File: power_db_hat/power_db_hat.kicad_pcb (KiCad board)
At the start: 2 copper layers, 65 x 56 mm, 161 parts, among them J1 GPIO, J10 Conn_01x04_Pin, J2 BAT1, J3 12V_out, J4 Conn_01x04_Pin, J5 24V_out, J6 PD_power, J7 Conn_01x20_Pin, J8 BAT2, J9 Conn_01x04_Pin, Q1 PMOS, Q2 PMOS, Q3 PMOS, Q5 PMOS, U1 INA3221, U2 TL431DBZ, U3 TPS54560BDDA, U4 TL431DBZ

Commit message: lol
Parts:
- removed C1, C10, C12, C18, C2, C3, C4, C5: 100nF, Capacitor_SMD:C_0805_2012Metric_Pad1.18x1.45mm_HandSolder
- removed D10, D14, D17, D18, D19, D20, D21, D22, D23, D24, D25, D26, D27, D28, D29, D30, D31, D32, D33, D34, D35, D36, D37, D38, D45, D46, D48, D50: TVS_3V3, Diode_SMD:D_0603_1608Metric_Pad1.05x0.95mm_HandSolder
- removed D11, D12, D13, D42, D9: TVS_13V, Diode_SMD:D_0603_1608Metric_Pad1.05x0.95mm_HandSolder
- removed D15, D16, D43, D8: TVS_26V, Diode_SMD:D_0603_1608Metric_Pad1.05x0.95mm_HandSolder
- removed D44, D47, D49, D51: TVS_5V, Diode_SMD:D_0603_1608Metric_Pad1.05x0.95mm_HandSolder
- removed F1: FUSE_10A, Fuse:Fuse_2512_6332Metric_Pad1.52x3.35mm_HandSolder
- removed F2: FUSE_5A, Fuse:Fuse_2512_6332Metric_Pad1.52x3.35mm_HandSolder
- removed J3: 12V_out, CONN_AMASS_3D_FIXED:AMASS_XT60PW-F_1x02_P7.20mm_Horizontal
- removed JP1, JP2, JP3, JP4: SolderJumper_2_Open, Jumper:SolderJumper-2_P1.3mm_Open_TrianglePad1.0x1.5mm
- removed L1: 8.2uH, Inductors_custom:VSHB0754T_Molded_Power_Choke
- removed Q1, Q2, Q5: PMOS, Package_TO_SOT_SMD:TO-252-3_TabPin2
- removed R1, R2, R3, R4: 0, Resistor_SMD:R_0603_1608Metric_Pad0.98x0.95mm_HandSolder
- removed R10, R11, R12, R13, R14: R, Resistor_SMD:R_0603_1608Metric_Pad0.98x0.95mm_HandSolder
- removed R15, R17: 12k, Resistor_SMD:R_0603_1608Metric_Pad0.98x0.95mm_HandSolder
- removed R16: 3k, Resistor_SMD:R_0603_1608Metric_Pad0.98x0.95mm_HandSolder
- removed R18, R28: 100, Resistor_SMD:R_0603_1608Metric_Pad0.98x0.95mm_HandSolder
- removed R21: 75k, Resistor_SMD:R_0603_1608Metric_Pad0.98x0.95mm_HandSolder
- removed R24: 2.2k, Resistor_SMD:R_0603_1608Metric_Pad0.98x0.95mm_HandSolder
- removed R25: 68k, Resistor_SMD:R_0603_1608Metric_Pad0.98x0.95mm_HandSolder
- removed R26, R6: 10k, Resistor_SMD:R_0603_1608Metric_Pad0.98x0.95mm_HandSolder
- removed R27, R32, R37, R39, R40, R41: 4.7k, Resistor_SMD:R_0603_1608Metric_Pad0.98x0.95mm_HandSolder
- removed R29: 200k, Resistor_SMD:R_0603_1608Metric_Pad0.98x0.95mm_HandSolder
- removed R45, R46, R47, R48, R49, R50, R51, R52, R53, R54, R55, R56, R57, R58, R59, R60, R61, R62, R63, R64: 33, Resistor_SMD:R_0603_1608Metric_Pad0.98x0.95mm_HandSolder
- removed R5, R7: 100k, Resistor_SMD:R_0603_1608Metric_Pad0.98x0.95mm_HandSolder
- removed U4: TL431DBZ, Package_TO_SOT_SMD:SOT-23
- added C27: 22uF, Capacitor_SMD:C_0603_1608Metric_Pad1.08x0.95mm_HandSolder, B.Cu at (141.3, 58.0)
- added C28: 22uF, Capacitor_SMD:C_0603_1608Metric_Pad1.08x0.95mm_HandSolder, B.Cu at (141.3, 60.5)
- added C29: 100nF, Capacitor_SMD:C_0603_1608Metric_Pad1.08x0.95mm_HandSolder, B.Cu at (141.3, 63.0)
- added C31: 100nF, Capacitor_SMD:C_0603_1608Metric_Pad1.08x0.95mm_HandSolder, B.Cu at (141.3, 65.5)
- added C32: 2.2uF, Capacitor_SMD:C_0603_1608Metric_Pad1.08x0.95mm_HandSolder, B.Cu at (141.3, 68.0)
- added C33: 22uF, Capacitor_SMD:C_0603_1608Metric_Pad1.08x0.95mm_HandSolder, B.Cu at (141.3, 70.6)
- added C34: 2.2uF, Capacitor_SMD:C_0603_1608Metric_Pad1.08x0.95mm_HandSolder, B.Cu at (137.0, 53.0)
- added C35: 100nF, Capacitor_SMD:C_0603_1608Metric_Pad1.08x0.95mm_HandSolder, B.Cu at (137.0, 55.5)
- added C36: 22nF, Capacitor_SMD:C_0603_1608Metric_Pad1.08x0.95mm_HandSolder, B.Cu at (137.0, 58.0)
- added C37: 100nF, Capacitor_SMD:C_0603_1608Metric_Pad1.08x0.95mm_HandSolder, B.Cu at (137.0, 60.5)
- added C38: 100nF, Capacitor_SMD:C_0603_1608Metric_Pad1.08x0.95mm_HandSolder, B.Cu at (137.0, 63.0)
- added C39: 22uF, Capacitor_SMD:C_0603_1608Metric_Pad1.08x0.95mm_HandSolder, B.Cu at (137.0, 65.5)
- added C40: 2.2uF, Capacitor_SMD:C_0603_1608Metric_Pad1.08x0.95mm_HandSolder, B.Cu at (137.0, 68.0)
- added C41: 22uF, Capacitor_SMD:C_0603_1608Metric_Pad1.08x0.95mm_HandSolder, B.Cu at (137.0, 70.6)
- added C42: 22uF, Capacitor_SMD:C_0603_1608Metric_Pad1.08x0.95mm_HandSolder, B.Cu at (132.6, 53.0)
- added C43: 22uF, Capacitor_SMD:C_0603_1608Metric_Pad1.08x0.95mm_HandSolder, B.Cu at (132.6, 55.5)
- added D52: D_Schottky, Diode_SMD:D_SMA-SMB_Universal_Handsoldering, B.Cu at (153.5, 83.1)
- added J11: Conn_01x03_Pin, Connector:FanPinHeader_1x03_P2.54mm_Vertical, F.Cu at (144.5, 48.0)
- added J12: Conn_01x03_Pin, Connector:FanPinHeader_1x03_P2.54mm_Vertical, F.Cu at (155.0, 48.0)
- added J15: Screw_Terminal_01x02, TerminalBlock:TerminalBlock_Xinya_XY308-2.54-2P_1x02_P2.54mm_Horizontal, F.Cu at (134.8, 48.3)
- added J16: Screw_Terminal_01x02, TerminalBlock:TerminalBlock_Xinya_XY308-2.54-2P_1x02_P2.54mm_Horizontal, F.Cu at (117.0, 95.5)
- added J17: Conn_02x06_Counter_Clockwise, Connector_PinSocket_2.54mm:PinSocket_2x06_P2.54mm_Vertical_SMD, B.Cu at (108.5, 85.5)
- added Q6: SIS468DN, Package_SO:Vishay_PowerPAK_1212-8_Single, B.Cu at (123.2, 54.2)
- added Q7: SIS468DN, Package_SO:Vishay_PowerPAK_1212-8_Single, B.Cu at (123.2, 58.9)
- added R65: 0, Resistor_SMD:R_0603_1608Metric_Pad0.98x0.95mm_HandSolder, B.Cu at (128.3, 68.0)
- added R66: 0, Resistor_SMD:R_0603_1608Metric_Pad0.98x0.95mm_HandSolder, B.Cu at (128.3, 70.6)
- added TP1: TestPoint, TestPoint:TestPoint_Pad_D1.0mm, F.Cu at (110.0, 50.0)
- added TP2: TestPoint, TestPoint:TestPoint_Pad_D1.0mm, F.Cu at (112.5, 50.0)
- added TP3: TestPoint, TestPoint:TestPoint_Pad_D1.0mm, F.Cu at (115.0, 50.0)
- added TP4: TestPoint, TestPoint:TestPoint_Pad_D1.0mm, F.Cu at (117.5, 50.0)
- added U5: MAX17506ATP+T, MAX17506:21-0140L_T2055-4_MXM, B.Cu at (126.5, 82.5)
- added U6: LDD-700LS, LD-700LS:SOP254P1280X930-16N, F.Cu at (141.1, 76.4)
- C11: value 4.7nF -> 2.2uF; moved to B.Cu
- C13: value 47pF -> 22uF; moved to B.Cu
- C14: value 100nF -> 2.2uF; footprint Capacitor_SMD:C_0805_2012Metric_Pad1.18x1.45mm_HandSolder -> Capacitor_SMD:C_0603_1608Metric_Pad1.08x0.95mm_HandSolder; moved to B.Cu
- C15: value 47uF -> 22nF; moved to B.Cu
- C16: value 47uF -> 100nF; moved to B.Cu
- C17: value 47uF -> 22uF; moved to B.Cu
- C6, C9: value 2.2uF -> 100nF; moved to B.Cu
- C7: moved to B.Cu
- C8: value 2.2uF -> 22uF; moved to B.Cu
- D1: value 3V3 -> LED_R; moved to F.Cu
- D2: value 5V -> LED_R; moved to F.Cu
- D3: value 12V -> LED_R; moved to F.Cu
- D4: value 24V -> LED_R; moved to F.Cu
- D5: value LED -> LED_R; moved to F.Cu
- D6: value B560C -> D_Schottky; footprint Diode_SMD:D_SMB-SMC_Universal_Handsoldering -> Diode_SMD:D_SMA-SMB_Universal_Handsoldering
- D7: value 12V -> TVS_26V
- J1: value GPIO -> Conn_01x02_Pin; footprint Connector_PinSocket_2.54mm:PinSocket_2x20_P2.54mm_Vertical -> TerminalBlock:TerminalBlock_Xinya_XY308-2.54-2P_1x02_P2.54mm_Horizontal; moved to F.Cu
- J10: value Conn_01x04_Pin -> Screw_Terminal_01x02; footprint Connector_JST:JST_GH_SM04B-GHS-TB_1x04-1MP_P1.25mm_Horizontal -> TerminalBlock:TerminalBlock_Xinya_XY308-2.54-2P_1x02_P2.54mm_Horizontal
- J2, J8: footprint CONN_AMASS_3D_FIXED:AMASS_XT60PW-M_1x02_P7.20mm_Horizontal -> AMASS_Custom:AMASS_XT60PW-M_1x02_P7.20mm_Horizontal
- J4: value Conn_01x04_Pin -> Screw_Terminal_01x02; footprint Connector_JST:JST_SH_SM04B-SRSS-TB_1x04-1MP_P1.00mm_Horizontal -> TerminalBlock:TerminalBlock_Xinya_XY308-2.54-2P_1x02_P2.54mm_Horizontal
- J5: footprint CONN_AMASS_3D_FIXED:AMASS_XT60PW-F_1x02_P7.20mm_Horizontal -> AMASS_Custom:AMASS_XT60PW-F_1x02_P7.20mm_Horizontal
- J6: value PD_power -> Conn_01x02_Pin; footprint Connector_JST:JST_GH_SM04B-GHS-TB_1x04-1MP_P1.25mm_Horizontal -> TerminalBlock:TerminalBlock_Xinya_XY308-2.54-2P_1x02_P2.54mm_Horizontal
- J7: value Conn_01x20_Pin -> Conn_02x06_Counter_Clockwise; footprint Connector_PinHeader_1.00mm:PinHeader_1x20_P1.00mm_Vertical -> Connector_PinSocket_2.54mm:PinSocket_2x06_P2.54mm_Vertical_SMD; moved to B.Cu
- J9: value Conn_01x04_Pin -> Conn_02x06_Counter_Clockwise; footprint Connector_JST:JST_GH_SM04B-GHS-TB_1x04-1MP_P1.25mm_Horizontal -> Connector_PinSocket_2.54mm:PinSocket_2x06_P2.54mm_Vertical_SMD; moved to B.Cu
- Q3: value PMOS -> AO4407A; footprint Package_TO_SOT_SMD:TO-252-3_TabPin2 -> Package_SO:SOIC-8-1EP_3.9x4.9mm_P1.27mm_EP2.41x3.81mm; moved to B.Cu
- R19: value 309k -> 4.7R; moved to B.Cu
- R20: value 53.6k -> 4.7R; moved to B.Cu
- R22: value 309k -> 162k; moved to B.Cu
- R23: value 14k -> 33.2k; moved to B.Cu
- R30: value 53.6k -> 10k; moved to B.Cu
- R31: value 10.2k -> 0; moved to B.Cu
- R35: value 4.7k -> 309k; moved to B.Cu
- R36: value 4.7k -> 24.9k; moved to B.Cu
- R38: value 4.7k -> 10k; moved to B.Cu
- R42, R43: value 33 -> 4.7R; moved to B.Cu
- R44: value 33 -> 0; moved to B.Cu
- U2: value TL431DBZ -> LDD-700LS; footprint Package_TO_SOT_SMD:SOT-23 -> LD-700LS:SOP254P1280X930-16N; moved to F.Cu
- U3: value TPS54560BDDA -> MAX17506ATP+T; footprint Package_SO:Texas_R-PDSO-G8_EP2.95x4.9mm_Mask2.4x3.1mm_ThermalVias -> MAX17506:21-0140L_T2055-4_MXM; moved to B.Cu
- moved D1 132.8 mm to (110.0, 47.0), turned to -90 degrees
- moved D2 130.7 mm to (112.5, 47.0), turned to -90 degrees
- moved D3 128.6 mm to (115.0, 47.0), turned to -90 degrees
- moved D4 126.6 mm to (117.5, 47.0), turned to -90 degrees
- moved D5 124.7 mm to (120.0, 47.0), turned to -90 degrees
- moved U2 121.7 mm to (142.2, 61.1), turned to 90 degrees
- moved R33 120.5 mm to (153.6, 70.0)
- moved R34 120.5 mm to (153.6, 74.9)
- moved R8 120.5 mm to (153.6, 65.1)
- moved U1 101.2 mm to (115.5, 66.5), turned to 0 degrees
- moved R38 84.3 mm to (128.3, 58.0), turned to 180 degrees
- moved R35 82.0 mm to (128.3, 53.0), turned to 180 degrees
- moved R36 82.0 mm to (128.3, 55.5), turned to 180 degrees
- moved R20 69.0 mm to (132.6, 60.5), turned to 180 degrees
- moved R23 68.2 mm to (132.6, 65.5), turned to 180 degrees
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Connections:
- C11 pad 1: GND -> /power/24V_SNS
- C11 pad 2: Net-(C11-Pad2) -> GND
- C13 pad 1: GND -> /power/24V_SNS
- C13 pad 2: Net-(U3-COMP) -> GND
- C14 pad 1: Net-(U3-BOOT) -> Net-(U3-VCC)
- C14 pad 2: Net-(D6-K) -> GND
- C15 pad 1: GND -> Net-(U3-SS)
- C15 pad 2: /power/5V_SNS -> GND
- C16 pad 1: GND -> Net-(U3-BST)
- C16 pad 2: /power/5V_SNS -> Net-(Q7-D)
- C17 pad 1: GND -> /power/bucks/BUCK_OUT_5V
- C17 pad 2: /power/5V_SNS -> GND
- C6 pad 1: /power/BUCK_IN -> /power/24V_SNS
- C7 pad 1: /power/BUCK_IN -> /power/24V_SNS
- C8 pad 1: /power/BUCK_IN -> /power/24V_SNS
- C9 pad 1: /power/BUCK_IN -> /power/24V_SNS
- D6 pad 1: Net-(D6-K) -> /power/5V_SNS
- D6 pad 2: GND -> /power/bucks/BUCK_OUT_5V
- J1 pad 1: +3V3 -> Net-(J1-Pin_1)
- J1 pad 2: +5V -> Net-(J1-Pin_2)
- J10 pad 1: /power/VIN_24V -> GND
- J10 pad 2: Net-(D16-A) -> GND
- J4 pad 1: GND -> +12V
- J4 pad 2: Net-(D36-K) -> GND
- J6 pad 1: /PD_VIN -> Net-(J6-Pin_1)
- J6 pad 2: GND -> Net-(J6-Pin_2)
- J7 pad 1: Net-(D14-K) -> GND
- J7 pad 10: Net-(D25-K) -> GND
- J7 pad 11: Net-(D26-K) -> GND
- J7 pad 12: Net-(D27-K) -> GND
- J7 pad 2: Net-(D17-K) -> /I2C_SDA
- J7 pad 3: Net-(D18-K) -> GND
- J7 pad 4: Net-(D19-K) -> GND
- J7 pad 5: Net-(D20-K) -> /IND_2
- J7 pad 6: Net-(D21-K) -> GND
- J7 pad 7: Net-(D22-K) -> /IND_3
- J7 pad 8: Net-(D23-K) -> GND
- J7 pad 9: Net-(D24-K) -> /IND_4
- J9 pad 1: /power/VIN_12V -> GND
- J9 pad 2: Net-(D13-K) -> /SERVO_1
- J9 pad 4: unconnected-(J9-Pin_4-Pad4) -> /SERVO_2
- R19 pad 1: /power/BUCK_IN -> Net-(U3-EXTVCC)
- R19 pad 2: Net-(U3-EN) -> /power/bucks/BUCK_OUT
- R20 pad 1: Net-(U3-EN) -> Net-(Q7-G)
- R20 pad 2: GND -> Net-(U3-DL)
- R22 pad 1: Net-(U3-RT/CLK) -> /power/bucks/BUCK_OUT_5V
- R22 pad 2: GND -> Net-(U3-FB)
- R23 pad 1: Net-(U3-COMP) -> Net-(U3-FB)
- R23 pad 2: Net-(C11-Pad2) -> GND
- R30 pad 1: /power/5V_SNS -> /power/bucks/BUCK_OUT_5V
- R30 pad 2: Net-(U3-FB) -> Net-(U3-*RESET)
- R31 pad 1: Net-(U3-FB) -> Net-(U3-EN/UVLO)
- R35 pad 1: /power/current/voltage_monitor/VDD -> /power/12V_SNS
- R35 pad 2: Net-(U1-SDA) -> Net-(U5-FB)
- R36 pad 1: /power/current/voltage_monitor/VDD -> Net-(U5-FB)
- R36 pad 2: Net-(U1-SCL) -> GND
- R38 pad 1: GND -> /power/12V_SNS
- R38 pad 2: Net-(U1-A0) -> Net-(U5-*RESET)
- R42 pad 1: /IVC_SW_2 -> Net-(U5-EXTVCC)
- R42 pad 2: Net-(D35-K) -> /power/12V_SNS
- R43 pad 1: /IVC_SW_1 -> Net-(Q6-G)
- R43 pad 2: Net-(D34-K) -> Net-(U5-DL)
- R44 pad 1: /IVC_SW_1_SOL -> Net-(U5-EN/UVLO)
- R44 pad 2: Net-(D33-K) -> GND
- U1 pad 16: /power/current/voltage_monitor/VDD -> +3V3
- U1 pad 5: Net-(U1-A0) -> Net-(JP5-A)
- U1 pad 6: Net-(U1-SCL) -> /I2C_SDA
- U1 pad 7: Net-(U1-SDA) -> GND
- U2 pad 1: Net-(U2-K) -> +24V
- U2 pad 2: Net-(U2-REF) -> Net-(J1-Pin_1)
- U2 pad 3: GND -> Net-(J1-Pin_1)
- U3 pad 1: Net-(U3-BOOT) -> /power/24V_SNS
- U3 pad 2: /power/BUCK_IN -> /power/24V_SNS
- U3 pad 3: Net-(U3-EN) -> GND
- U3 pad 4: Net-(U3-RT/CLK) -> Net-(U3-VCC)
- U3 pad 5: Net-(U3-FB) -> unconnected-(U3-MODE/SYNC-Pad5)
- U3 pad 6: Net-(U3-COMP) -> Net-(U3-*RESET)
- U3 pad 7: GND -> unconnected-(U3-RT-Pad7)
- U3 pad 8: Net-(D6-K) -> GND
- U3 pad 9: GND -> unconnected-(U3-CF-Pad9)
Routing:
- net /VBAT1+: track 13.8 -> 0.00 mm
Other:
- board text added: "24V"
- board text added: "BAT 1"
- board text added: "BAT 2"
- board text added: "LED1"
- board text added: "LED2"
- board text added: "SWITCH"
- board text added: "Servo1"
- board text added: "Servo2"
- board text removed: "DISPLAY (OPTIONAL)"

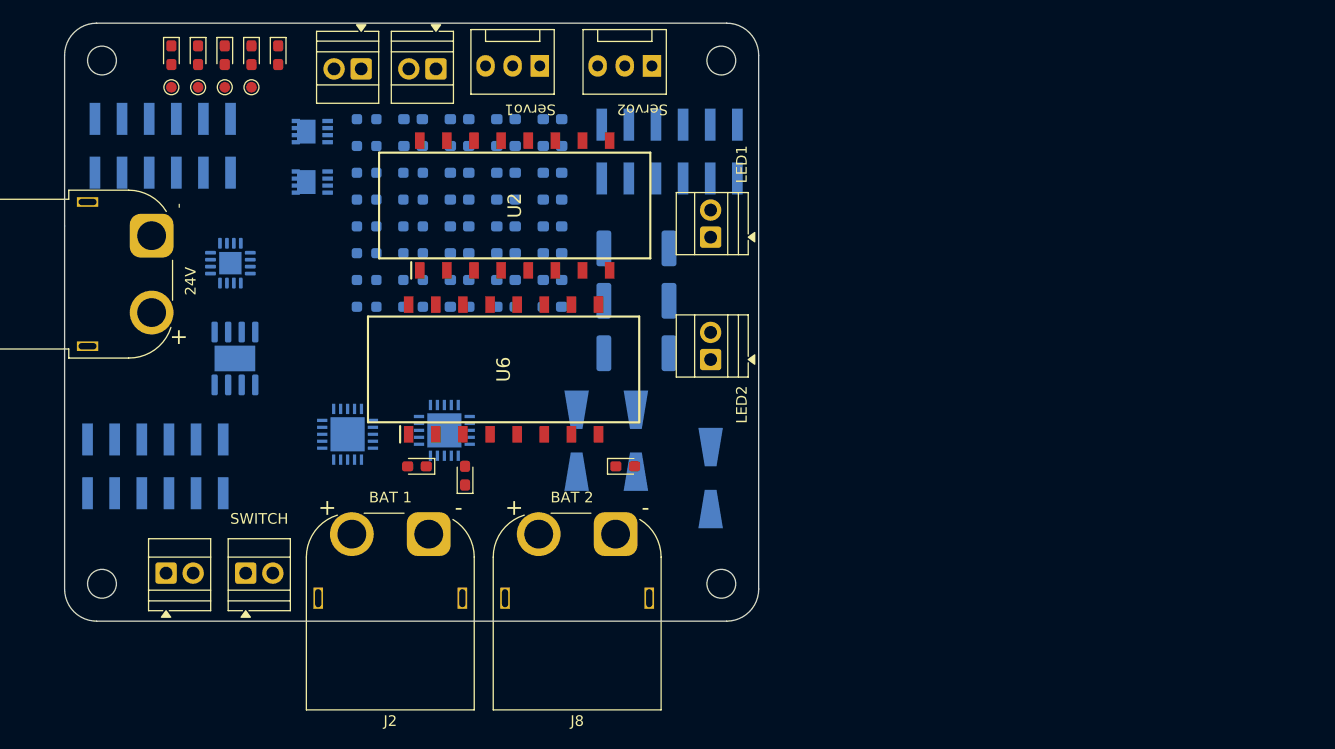
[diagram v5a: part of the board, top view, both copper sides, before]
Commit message: made b2b footprint
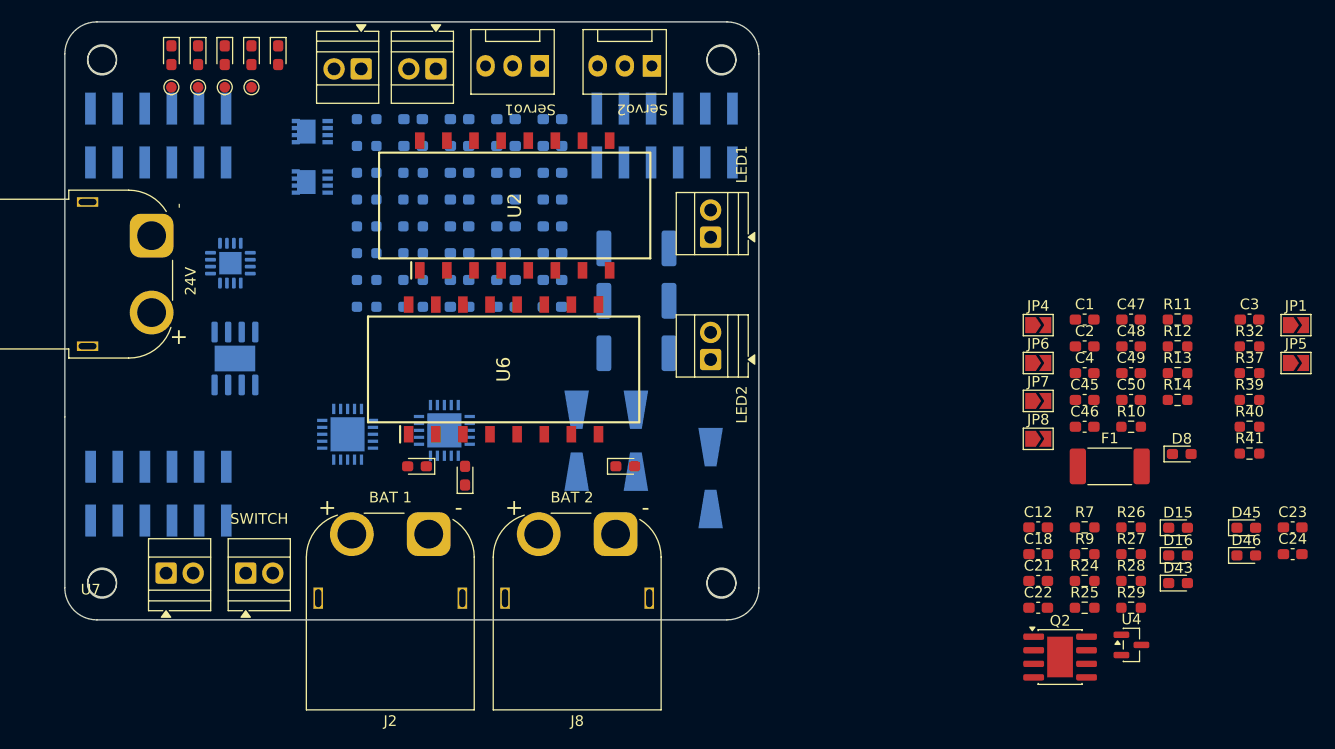
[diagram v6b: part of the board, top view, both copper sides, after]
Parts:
- removed J17, J7, J9: Conn_02x06_Counter_Clockwise, Connector_PinSocket_2.54mm:PinSocket_2x06_P2.54mm_Vertical_SMD
- added C1: 100nF, Capacitor_SMD:C_0603_1608Metric_Pad1.08x0.95mm_HandSolder, F.Cu at (195.5, 71.8)
- added C12: 100nF, Capacitor_SMD:C_0603_1608Metric_Pad1.08x0.95mm_HandSolder, F.Cu at (191.2, 91.2)
- added C18: 100nF, Capacitor_SMD:C_0603_1608Metric_Pad1.08x0.95mm_HandSolder, F.Cu at (191.2, 93.7)
- added C2: 100nF, Capacitor_SMD:C_0603_1608Metric_Pad1.08x0.95mm_HandSolder, F.Cu at (195.5, 74.3)
- added C21: 100nF, Capacitor_SMD:C_0603_1608Metric_Pad1.08x0.95mm_HandSolder, F.Cu at (191.2, 96.2)
- added C22: 100nF, Capacitor_SMD:C_0603_1608Metric_Pad1.08x0.95mm_HandSolder, F.Cu at (191.2, 98.7)
- added C23: 100nF, Capacitor_SMD:C_0603_1608Metric_Pad1.08x0.95mm_HandSolder, F.Cu at (215.0, 91.2)
- added C24: 100nF, Capacitor_SMD:C_0603_1608Metric_Pad1.08x0.95mm_HandSolder, F.Cu at (215.0, 93.7)
- added C3: 100nF, Capacitor_SMD:C_0603_1608Metric_Pad1.08x0.95mm_HandSolder, F.Cu at (211.0, 71.8)
- added C4: 100nF, Capacitor_SMD:C_0603_1608Metric_Pad1.08x0.95mm_HandSolder, F.Cu at (195.5, 76.8)
- added C45: 100nF, Capacitor_SMD:C_0603_1608Metric_Pad1.08x0.95mm_HandSolder, F.Cu at (195.5, 79.3)
- added C46: 22uF, Capacitor_SMD:C_0603_1608Metric_Pad1.08x0.95mm_HandSolder, F.Cu at (195.5, 81.8)
- added C47: 100nF, Capacitor_SMD:C_0603_1608Metric_Pad1.08x0.95mm_HandSolder, F.Cu at (199.9, 71.8)
- added C48: 22uF, Capacitor_SMD:C_0603_1608Metric_Pad1.08x0.95mm_HandSolder, F.Cu at (199.9, 74.3)
- added C49: 100nF, Capacitor_SMD:C_0603_1608Metric_Pad1.08x0.95mm_HandSolder, F.Cu at (199.9, 76.8)
- added C50: 22uF, Capacitor_SMD:C_0603_1608Metric_Pad1.08x0.95mm_HandSolder, F.Cu at (199.9, 79.3)
- added D15: TVS_26V, Diode_SMD:D_0603_1608Metric_Pad1.05x0.95mm_HandSolder, F.Cu at (204.3, 91.3)
- added D16: TVS_26V, Diode_SMD:D_0603_1608Metric_Pad1.05x0.95mm_HandSolder, F.Cu at (204.3, 93.8)
- added D43: TVS_26V, Diode_SMD:D_0603_1608Metric_Pad1.05x0.95mm_HandSolder, F.Cu at (204.3, 96.4)
- added D45: TVS_3V3, Diode_SMD:D_0603_1608Metric_Pad1.05x0.95mm_HandSolder, F.Cu at (210.7, 91.3)
- added D46: TVS_3V3, Diode_SMD:D_0603_1608Metric_Pad1.05x0.95mm_HandSolder, F.Cu at (210.7, 93.8)
- added D8: TVS_26V, Diode_SMD:D_0603_1608Metric_Pad1.05x0.95mm_HandSolder, F.Cu at (204.6, 84.3)
- added F1: FUSE_10A, Fuse:Fuse_2512_6332Metric_Pad1.52x3.35mm_HandSolder, F.Cu at (197.9, 85.5)
- added JP1: SolderJumper_2_Open, Jumper:SolderJumper-2_P1.3mm_Open_TrianglePad1.0x1.5mm, F.Cu at (215.3, 72.3)
- added JP4: SolderJumper_2_Open, Jumper:SolderJumper-2_P1.3mm_Open_TrianglePad1.0x1.5mm, F.Cu at (191.2, 72.3)
- added JP5: SolderJumper_2_Open, Jumper:SolderJumper-2_P1.3mm_Open_TrianglePad1.0x1.5mm, F.Cu at (215.3, 75.8)
- added JP6: SolderJumper_2_Open, Jumper:SolderJumper-2_P1.3mm_Open_TrianglePad1.0x1.5mm, F.Cu at (191.2, 75.8)
- added JP7: SolderJumper_2_Open, Jumper:SolderJumper-2_P1.3mm_Open_TrianglePad1.0x1.5mm, F.Cu at (191.2, 79.4)
- added JP8: SolderJumper_2_Open, Jumper:SolderJumper-2_P1.3mm_Open_TrianglePad1.0x1.5mm, F.Cu at (191.2, 82.9)
- added Q2: AO4407A, Package_SO:SOIC-8-1EP_3.9x4.9mm_P1.27mm_EP2.41x3.81mm, F.Cu at (193.2, 103.4)
- added R10: 330, Resistor_SMD:R_0603_1608Metric_Pad0.98x0.95mm_HandSolder, F.Cu at (199.9, 81.8)
- added R11: 1k, Resistor_SMD:R_0603_1608Metric_Pad0.98x0.95mm_HandSolder, F.Cu at (204.2, 71.8)
- added R12: 4.7k, Resistor_SMD:R_0603_1608Metric_Pad0.98x0.95mm_HandSolder, F.Cu at (204.2, 74.3)
- added R13: 10k, Resistor_SMD:R_0603_1608Metric_Pad0.98x0.95mm_HandSolder, F.Cu at (204.2, 76.8)
- added R14: 330, Resistor_SMD:R_0603_1608Metric_Pad0.98x0.95mm_HandSolder, F.Cu at (204.2, 79.3)
- added R24: 2.2k, Resistor_SMD:R_0603_1608Metric_Pad0.98x0.95mm_HandSolder, F.Cu at (195.5, 96.2)
- added R25: 68k, Resistor_SMD:R_0603_1608Metric_Pad0.98x0.95mm_HandSolder, F.Cu at (195.5, 98.7)
- added R26: 10k, Resistor_SMD:R_0603_1608Metric_Pad0.98x0.95mm_HandSolder, F.Cu at (199.9, 91.2)
- added R27: 4.7k, Resistor_SMD:R_0603_1608Metric_Pad0.98x0.95mm_HandSolder, F.Cu at (199.9, 93.7)
- added R28: 100, Resistor_SMD:R_0603_1608Metric_Pad0.98x0.95mm_HandSolder, F.Cu at (199.9, 96.2)
- added R29: 200k, Resistor_SMD:R_0603_1608Metric_Pad0.98x0.95mm_HandSolder, F.Cu at (199.9, 98.7)
- added R32: 4.7k, Resistor_SMD:R_0603_1608Metric_Pad0.98x0.95mm_HandSolder, F.Cu at (211.0, 74.3)
- added R37: 10k, Resistor_SMD:R_0603_1608Metric_Pad0.98x0.95mm_HandSolder, F.Cu at (211.0, 76.8)
- added R39: 4.7k, Resistor_SMD:R_0603_1608Metric_Pad0.98x0.95mm_HandSolder, F.Cu at (211.0, 79.3)
- added R40: 4.7k, Resistor_SMD:R_0603_1608Metric_Pad0.98x0.95mm_HandSolder, F.Cu at (211.0, 81.8)
- added R41: 4.7k, Resistor_SMD:R_0603_1608Metric_Pad0.98x0.95mm_HandSolder, F.Cu at (211.0, 84.3)
- added R7: 100k, Resistor_SMD:R_0603_1608Metric_Pad0.98x0.95mm_HandSolder, F.Cu at (195.5, 91.2)
- added R9: 10k, Resistor_SMD:R_0603_1608Metric_Pad0.98x0.95mm_HandSolder, F.Cu at (195.5, 93.7)
- added U4: TL431DBZ, Package_TO_SOT_SMD:SOT-23, F.Cu at (199.9, 102.2)
- added U7: B2B pins, B2B-Connectors:B2B_pin_socket_3x(02x06), F.Cu at (102.4, 99.0)
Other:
- outline, holes or cut-outs redrawn

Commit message: lol
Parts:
- moved U1 83.5 mm to (195.7, 89.8)
- moved Q3 83.5 mm to (196.2, 98.7)
- moved C11 67.3 mm to (212.9, 66.6)
- moved C13 67.3 mm to (212.9, 69.1)
- moved C14 67.3 mm to (212.9, 71.6)
- moved C15 67.3 mm to (212.9, 74.1)
- moved C6 67.3 mm to (212.9, 56.6)
- moved C7 67.3 mm to (212.9, 59.1)
- moved C8 67.3 mm to (212.9, 61.6)
- moved C9 67.3 mm to (212.9, 64.1)
- moved D6 57.5 mm to (186.7, 40.6)
- moved D52 57.5 mm to (192.2, 40.6)
- moved C16 56.5 mm to (197.7, 56.4)
- moved C17 56.5 mm to (197.7, 59.0)
- moved C27 56.5 mm to (197.7, 61.5)
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
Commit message: update
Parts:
- removed D16: TVS_26V, Diode_SMD:D_0603_1608Metric_Pad1.05x0.95mm_HandSolder
- removed D39, D40: TVS_13V, Diode_SMD:D_0603_1608Metric_Pad1.05x0.95mm_HandSolder
- removed JP7, JP8: SolderJumper_2_Open, Jumper:SolderJumper-2_P1.3mm_Open_TrianglePad1.0x1.5mm
- removed Q3: AO4407A, Package_SO:SOIC-8-1EP_3.9x4.9mm_P1.27mm_EP2.41x3.81mm
- added C10: 100nF, Capacitor_SMD:C_0603_1608Metric_Pad1.08x0.95mm_HandSolder, F.Cu at (238.2, 121.8)
- added C19: 22uF, Capacitor_SMD:C_0603_1608Metric_Pad1.08x0.95mm_HandSolder, F.Cu at (238.2, 124.3)
- added C20: 100nF, Capacitor_SMD:C_0603_1608Metric_Pad1.08x0.95mm_HandSolder, F.Cu at (238.2, 126.8)
- added C25: 100nF, Capacitor_SMD:C_0603_1608Metric_Pad1.08x0.95mm_HandSolder, F.Cu at (238.2, 129.3)
- added C26: 22uF, Capacitor_SMD:C_0603_1608Metric_Pad1.08x0.95mm_HandSolder, F.Cu at (238.2, 131.8)
- added C30: 100nF, Capacitor_SMD:C_0603_1608Metric_Pad1.08x0.95mm_HandSolder, F.Cu at (238.2, 134.3)
- added C44: 100nF, Capacitor_SMD:C_0603_1608Metric_Pad1.08x0.95mm_HandSolder, F.Cu at (238.2, 136.8)
- added C5: 100nF, Capacitor_SMD:C_0603_1608Metric_Pad1.08x0.95mm_HandSolder, F.Cu at (238.2, 119.3)
- added D10: TVS_26V, Diode_SMD:D_SMB_Handsoldering, B.Cu at (113.5, 118.1)
- added D11: D_Zener, Diode_SMD:D_0603_1608Metric_Pad1.05x0.95mm_HandSolder, F.Cu at (120.0, 89.0)
- added D9: TVS_13V, Diode_SMD:D_SMB_Handsoldering, B.Cu at (137.0, 84.0)
- added J3: Screw_Terminal_01x02, TerminalBlock:TerminalBlock_Xinya_XY308-2.54-2P_1x02_P2.54mm_Horizontal, F.Cu at (160.5, 80.0)
- added J7: Screw_Terminal_01x02, TerminalBlock:TerminalBlock_Xinya_XY308-2.54-2P_1x02_P2.54mm_Horizontal, F.Cu at (160.5, 87.5)
- added JP10: SolderJumper_2_Open, Jumper:SolderJumper-2_P1.3mm_Open_TrianglePad1.0x1.5mm, F.Cu at (181.7, 134.5)
- added JP11: SolderJumper_2_Open, Jumper:SolderJumper-2_P1.3mm_Open_TrianglePad1.0x1.5mm, F.Cu at (181.7, 119.9)
- added JP12: SolderJumper_2_Open, Jumper:SolderJumper-2_P1.3mm_Open_TrianglePad1.0x1.5mm, F.Cu at (181.7, 123.4)
- added JP2: SolderJumper_2_Open, Jumper:SolderJumper-2_P1.3mm_Open_TrianglePad1.0x1.5mm, F.Cu at (181.7, 112.8)
- added JP3: SolderJumper_2_Open, Jumper:SolderJumper-2_P1.3mm_Open_TrianglePad1.0x1.5mm, F.Cu at (181.7, 116.3)
- added JP9: SolderJumper_2_Open, Jumper:SolderJumper-2_P1.3mm_Open_TrianglePad1.0x1.5mm, F.Cu at (181.7, 131.0)
- added L1: 4.7uH, IND_B82477G4472M000:IND_B82477G4472M000, F.Cu at (120.2, 60.8)
- added L2: 10uH, IND_B82477G4472M000:IND_B82477G4472M000, F.Cu at (210.5, 105.8)
- added Q1: FDS6681Z, FDS6681Z:FDS6681Z_SOP-8, F.Cu at (113.7, 87.5)
- added R1: 10k, Resistor_SMD:R_0603_1608Metric_Pad0.98x0.95mm_HandSolder, F.Cu at (238.2, 139.3)
- added R2: 10k, Resistor_SMD:R_0603_1608Metric_Pad0.98x0.95mm_HandSolder, F.Cu at (238.2, 141.8)
- added U8: DRV8212P, Package_SON:WSON-8-1EP_2x2mm_P0.5mm_EP0.9x1.6mm_ThermalVias, F.Cu at (186.1, 121.7)
- added U9: DRV8212P, Package_SON:WSON-8-1EP_2x2mm_P0.5mm_EP0.9x1.6mm_ThermalVias, F.Cu at (192.1, 126.2)
- C3, F1, JP1, JP5, R32, R37, R39, R40, R41: moved to B.Cu
- D6: footprint Diode_SMD:D_SMA-SMB_Universal_Handsoldering -> Diode_SMD:D_SMB_Handsoldering
- D7: value TVS_26V -> D_Zener; footprint Diode_SMD:D_SMA-SMB_Universal_Handsoldering -> Diode_SMD:D_0603_1608Metric_Pad1.05x0.95mm_HandSolder; moved to F.Cu
- D8: value TVS_26V -> TVS_13V; footprint Diode_SMD:D_0603_1608Metric_Pad1.05x0.95mm_HandSolder -> Diode_SMD:D_SMB_Handsoldering; moved to B.Cu
- J2: value BAT1 -> BAT2
- J8: value BAT2 -> BAT1
- Q2: value AO4407A -> FDS6681Z; footprint Package_SO:SOIC-8-1EP_3.9x4.9mm_P1.27mm_EP2.41x3.81mm -> FDS6681Z:FDS6681Z_SOP-8
- U1: moved to F.Cu
- moved C14 96.3 mm to (116.8, 66.2), turned to 90 degrees
- moved R29 94.4 mm to (107.2, 80.5)
- moved R28 93.7 mm to (107.2, 82.2), turned to 180 degrees
- moved U4 90.9 mm to (111.2, 82.0), turned to -90 degrees
- moved Q2 89.9 mm to (105.0, 86.1), turned to 180 degrees
- moved C18 89.0 mm to (102.2, 91.2), turned to -90 degrees
- moved R26 86.6 mm to (114.2, 78.2), turned to 90 degrees
- moved C22 86.5 mm to (105.0, 91.2), turned to -90 degrees
- moved R27 86.4 mm to (114.2, 82.0), turned to 90 degrees
- moved C7 85.3 mm to (127.7, 62.8), turned to 90 degrees
- moved D15 84.3 mm to (120.0, 90.8)
- moved D43 83.2 mm to (121.8, 85.5)
- moved C6 82.9 mm to (130.2, 62.8), turned to 90 degrees
- moved R25 82.1 mm to (116.0, 78.2), turned to -90 degrees
- moved C8 80.4 mm to (132.8, 68.0), turned to 90 degrees
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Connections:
- C11 pad 1: /power/24V_SNS -> +24V
- C13 pad 1: /power/24V_SNS -> +24V
- C21 pad 1: /power/VIN_24V -> /VBAT_24V
- C31 pad 1: /power/24V_SNS -> +24V
- C32 pad 1: /power/24V_SNS -> +24V
- C33 pad 1: /power/24V_SNS -> +24V
- C38 pad 1: /power/24V_SNS -> +24V
- C40 pad 1: /power/24V_SNS -> +24V
- C42 pad 1: /power/24V_SNS -> +24V
- C47 pad 1: Net-(C47-Pad1) -> GND
- C48 pad 2: Net-(C47-Pad1) -> GND
- C6 pad 1: /power/24V_SNS -> +24V
- C7 pad 1: /power/24V_SNS -> +24V
- C8 pad 1: /power/24V_SNS -> +24V
- C9 pad 1: /power/24V_SNS -> +24V
- D15 pad 1: /power/VIN_24V -> /VBAT_24V
- D41 pad 1: /VBAT2+ -> /VBAT_24V
- D43 pad 1: Net-(D16-A) -> Net-(D11-A)
- D7 pad 1: Net-(D7-K) -> /power/24V_SWITCH
- D7 pad 2: /power/24V_SWITCH -> Net-(D7-A)
- D8 pad 1: Net-(D8-K) -> /VBAT1+
- D8 pad 2: GND -> /VBAT2+
- F1 pad 1: Net-(D8-K) -> /VBAT2+
- F1 pad 2: +24V -> /VBAT_24V
- J16 pad 1: Net-(D16-A) -> /VBAT_24V
- J16 pad 2: /power/VIN_24V -> Net-(D11-A)
- Q2 pad 1: /power/24V_SNS -> /power/24V_SWITCH
- Q2 pad 3: /power/24V_SWITCH -> /power/24V_SNS
- R27 pad 2: Net-(D7-K) -> Net-(D7-A)
- R28 pad 1: Net-(D7-K) -> Net-(D7-A)
- R65 pad 1: /power/24V_SNS -> Net-(JP10-A)
- R66 pad 1: /power/24V_SNS -> Net-(JP9-A)
- R7 pad 1: /power/VIN_24V -> /VBAT_24V
- R7 pad 2: Net-(D16-A) -> Net-(D11-A)
- R8 pad 1: /power/VOUT_24V -> +24V
- R9 pad 1: Net-(D16-A) -> Net-(D11-A)
- U1 pad 11: /power/VOUT_24V -> +24V
- U1 pad 7: GND -> /I2C_SCL
- U2 pad 10: Net-(J1-Pin_1) -> Net-(J1-Pin_2)
- U2 pad 11: Net-(J1-Pin_1) -> Net-(J1-Pin_2)
- U2 pad 12: Net-(J1-Pin_1) -> Net-(J1-Pin_2)
- U2 pad 13: Net-(J1-Pin_1) -> Net-(J1-Pin_2)
- U2 pad 14: GND -> /LED_PWM_1
- U2 pad 15: Net-(J1-Pin_1) -> Net-(J1-Pin_2)
- U2 pad 2: Net-(J1-Pin_1) -> Net-(J1-Pin_2)
- U2 pad 3: Net-(J1-Pin_1) -> Net-(J1-Pin_2)
- U2 pad 4: Net-(J1-Pin_1) -> Net-(J1-Pin_2)
- U2 pad 5: Net-(J1-Pin_1) -> Net-(J1-Pin_2)
- U2 pad 6: Net-(J1-Pin_1) -> Net-(J1-Pin_2)
- U2 pad 7: Net-(J1-Pin_2) -> Net-(J1-Pin_1)
- U2 pad 8: Net-(J1-Pin_2) -> Net-(J1-Pin_1)
- U2 pad 9: Net-(J1-Pin_1) -> Net-(J1-Pin_2)
- U3 pad 1: /power/24V_SNS -> +24V
- U3 pad 14: /power/24V_SNS -> +24V
- U3 pad 15: /power/24V_SNS -> +24V
- U3 pad 2: /power/24V_SNS -> +24V
- U4 pad 1: Net-(D7-K) -> Net-(D7-A)
- U5 pad 1: /power/24V_SNS -> +24V
- U5 pad 14: /power/24V_SNS -> +24V
- U5 pad 15: /power/24V_SNS -> +24V
- U5 pad 2: /power/24V_SNS -> +24V
- U6 pad 10: Net-(J6-Pin_1) -> Net-(J6-Pin_2)
- U6 pad 11: Net-(J6-Pin_1) -> Net-(J6-Pin_2)
- U6 pad 12: Net-(J6-Pin_1) -> Net-(J6-Pin_2)
- U6 pad 13: Net-(J6-Pin_1) -> Net-(J6-Pin_2)
- U6 pad 14: GND -> /LED_PWM_2
- U6 pad 15: Net-(J6-Pin_1) -> Net-(J6-Pin_2)
- U6 pad 2: Net-(J6-Pin_1) -> Net-(J6-Pin_2)
- U6 pad 3: Net-(J6-Pin_1) -> Net-(J6-Pin_2)
- U6 pad 4: Net-(J6-Pin_1) -> Net-(J6-Pin_2)
- U6 pad 5: Net-(J6-Pin_1) -> Net-(J6-Pin_2)
- U6 pad 6: Net-(J6-Pin_1) -> Net-(J6-Pin_2)
- U6 pad 7: Net-(J6-Pin_2) -> Net-(J6-Pin_1)
- U6 pad 8: Net-(J6-Pin_2) -> Net-(J6-Pin_1)
- U6 pad 9: Net-(J6-Pin_1) -> Net-(J6-Pin_2)
- U7 pad 10a: +5V -> GND
- U7 pad 11a: Net-(C47-Pad1) -> +12V
- U7 pad 11b: GND -> +3V3
- U7 pad 11c: GND -> /LED_PWM_2
- U7 pad 12a: +5V -> GND
- U7 pad 12b: GND -> /I2C_SCL
- U7 pad 1a: +12V -> GND
- U7 pad 1b: GND -> +5V
- U7 pad 1c: GND -> /MOTOR_1_A
- U7 pad 2a: +3V3 -> GND
- U7 pad 2b: /I2C_SDA -> +5V
- U7 pad 3a: +12V -> GND
- U7 pad 3b: GND -> +5V
- U7 pad 3c: GND -> /MOTOR_1_B
- U7 pad 4a: +3V3 -> GND
- U7 pad 4b: GND -> +5V
- U7 pad 5b: /IND_2 -> +5V
- U7 pad 5c: GND -> /MOTOR_2_A
- U7 pad 6a: +5V -> GND
- U7 pad 7b: /IND_3 -> +5V
- U7 pad 7c: GND -> /MOTOR_2_B
- U7 pad 8a: +5V -> GND
- U7 pad 8b: GND -> /I2C_SDA
- U7 pad 9a: GND -> +12V
- U7 pad 9b: /IND_4 -> +3V3
- U7 pad 9c: GND -> /LED_PWM_1
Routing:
- net Net-(J6-Pin_2): track 0.00 -> 52.0 mm
- net Net-(J1-Pin_2): track 0.00 -> 48.5 mm
- net Net-(J1-Pin_1): track 0.00 -> 15.9 mm
- net Net-(D11-A): track 0.00 -> 14.0 mm
- net /power/24V_SWITCH: track 0.00 -> 12.9 mm
- net Net-(J6-Pin_1): track 0.00 -> 12.6 mm
- net Net-(D7-A): track 0.00 -> 12.0 mm
- net Net-(U4-REF): track 0.00 -> 7.93 mm
- net Net-(Q1-G): track 0.00 -> 4.98 mm
- net +24V: track 0.00 -> 3.16 mm, vias 0 -> 22
- net Net-(R24-Pad2): track 0.00 -> 2.72 mm
- net Net-(U3-VCC): track 0.00 -> 2.53 mm
- net /power/24V_SNS: track 0.00 -> 2.48 mm, vias 0 -> 15
- net Net-(Q2-G): track 0.00 -> 2.44 mm
- net /VBAT_24V: track 0.00 -> 2.03 mm
- added copper zone on B.Cu, net +24V
- added copper zone on In1.Cu, net +24V
- added copper zone on B.Cu, net /VBAT1+
- added copper zone on B.Cu, net /VBAT2+
- added copper zone on B.Cu, net /VBAT_24V
- added copper zone on F.Cu, net /VBAT_24V
- added copper zone on B.Cu, net /power/24V_SNS
- added copper zone on F.Cu, net /power/24V_SNS
- added copper zone on F.Cu, net /power/24V_SWITCH
- added copper zone on In2.Cu, net GND
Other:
- copper layers 2 -> 4
- board text added: "ACT1"
- board text added: "ACT2"
- board text removed: "USB"
